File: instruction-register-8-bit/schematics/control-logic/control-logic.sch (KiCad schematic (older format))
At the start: 6 parts

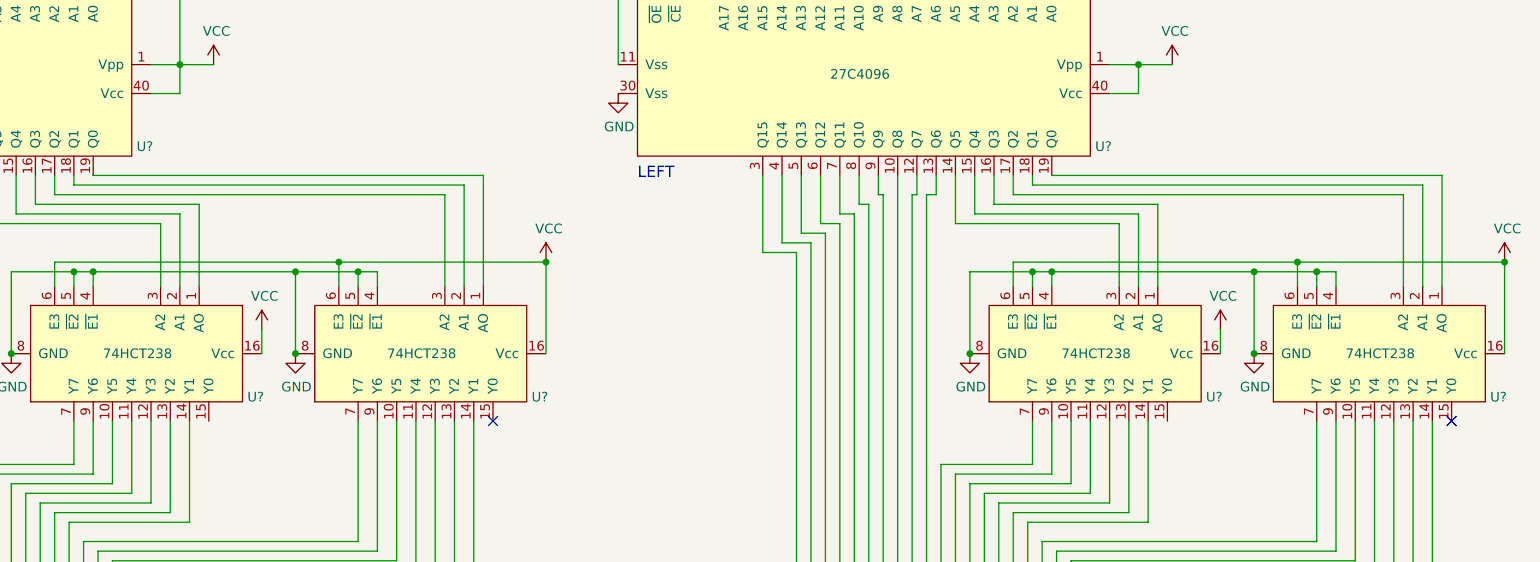
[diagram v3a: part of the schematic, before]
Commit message: removed A16 address line
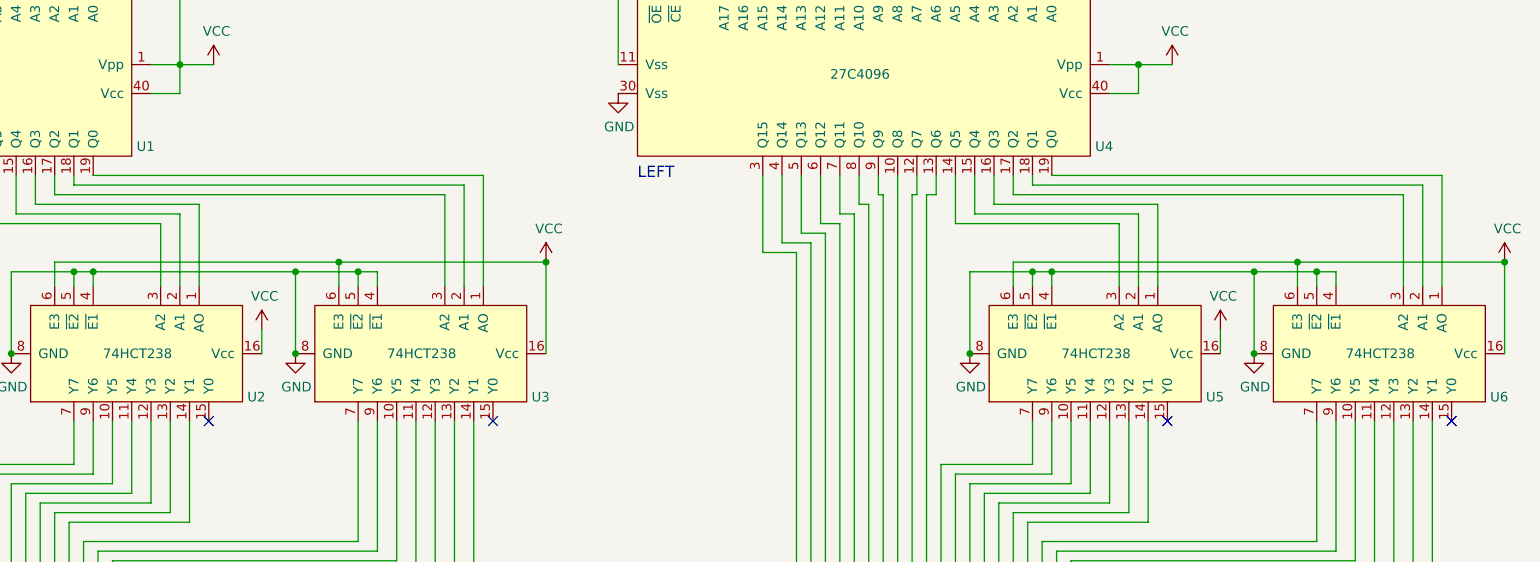
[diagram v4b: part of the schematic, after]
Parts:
- gave numbers to parts that had none: 6
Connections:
- no-connect marks 2 -> 4
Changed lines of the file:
@@
 $EndDescr
 $Comp
-L common-symbols:74HCT238 U?
+L common-symbols:74HCT238 U3
 U 1 1 60DA7B46
 P 5450 4825
-F 0 "U?" V 5675 5375 50  0000 L CNN
+F 0 "U3" V 5675 5375 50  0000 L CNN
 F 1 "74HCT238" V 5450 4625 50  0000 L CNN
 F 2 "" H 5300 4650 50  0001 C CNN
@@
 $EndComp
 $Comp
-L common-symbols:74HCT238 U?
+L common-symbols:74HCT238 U2
 U 1 1 60D8B240
 P 3975 4825
-F 0 "U?" V 4200 5375 50  0000 L CNN
+F 0 "U2" V 4200 5375 50  0000 L CNN
 F 1 "74HCT238" V 3975 4625 50  0000 L CNN
 F 2 "" H 3825 4650 50  0001 C CNN
@@
 CL_48
 $Comp
-L power:GND #PWR?
+L power:GND #PWR01
 U 1 1 60E3EE03
 P 1475 3475
-F 0 "#PWR?" H 1475 3225 50  0001 C CNN
+F 0 "#PWR01" H 1475 3225 50  0001 C CNN
 F 1 "GND" H 1480 3302 50  0000 C CNN
 F 2 "" H 1475 3475 50  0001 C CNN
@@
 $EndComp
 $Comp
-L power:GND #PWR?
+L power:GND #PWR05
 U 1 1 60E3F44C
 P 4775 4825
-F 0 "#PWR?" H 4775 4575 50  0001 C CNN
+F 0 "#PWR05" H 4775 4575 50  0001 C CNN
 F 1 "GND" H 4780 4652 50  0000 C CNN
 F 2 "" H 4775 4825 50  0001 C CNN
@@
 $EndComp
 $Comp
-L power:VCC #PWR?
+L power:VCC #PWR04
 U 1 1 60E3F8E0
 P 4600 4700
-F 0 "#PWR?" H 4600 4550 50  0001 C CNN
+F 0 "#PWR04" H 4600 4550 50  0001 C CNN
 F 1 "VCC" H 4615 4873 50  0000 C CNN
 F 2 "" H 4600 4700 50  0001 C CNN
@@
 	4600 4825 4600 4700
 $Comp
-L power:VCC #PWR?
+L power:VCC #PWR06
 U 1 1 60E4BA0B
 P 6075 4350
-F 0 "#PWR?" H 6075 4200 50  0001 C CNN
+F 0 "#PWR06" H 6075 4200 50  0001 C CNN
 F 1 "VCC" H 6090 4523 50  0000 C CNN
 F 2 "" H 6075 4350 50  0001 C CNN
@@
 	4175 3325 4350 3325
 $Comp
-L power:VCC #PWR?
+L power:VCC #PWR03
 U 1 1 6128F265
 P 4350 3325
-F 0 "#PWR?" H 4350 3175 50  0001 C CNN
+F 0 "#PWR03" H 4350 3175 50  0001 C CNN
 F 1 "VCC" H 4365 3498 50  0000 C CNN
 F 2 "" H 4350 3325 50  0001 C CNN
@@
 	1475 2800 1475 3325
 $Comp
-L common-symbols:27C4096 U?
+L common-symbols:27C4096 U1
 U 1 1 60DAC648
 P 3925 2975
-F 0 "U?" V 4700 3000 50  0000 L CNN
+F 0 "U1" V 4700 3000 50  0000 L CNN
 F 1 "27C4096" V 4325 1625 50  0000 L CNN
 F 2 "" H 4000 2900 50  0001 C CNN
@@
 Connection ~ 5100 4400
 $Comp
-L power:GND #PWR?
+L power:GND #PWR02
 U 1 1 6126E82E
 P 3300 4825
-F 0 "#PWR?" H 3300 4575 50  0001 C CNN
+F 0 "#PWR02" H 3300 4575 50  0001 C CNN
 F 1 "GND" H 3305 4652 50  0000 C CNN
 F 2 "" H 3300 4825 50  0001 C CNN
@@
 	3600 5700 4225 5700
 $Comp
-L common-symbols:74HCT238 U?
+L common-symbols:74HCT238 U6
 U 1 1 61437C3F
 P 10425 4825
-F 0 "U?" V 10650 5375 50  0000 L CNN
+F 0 "U6" V 10650 5375 50  0000 L CNN
 F 1 "74HCT238" V 10425 4625 50  0000 L CNN
 F 2 "" H 10275 4650 50  0001 C CNN
@@
 $EndComp
 $Comp
-L common-symbols:74HCT238 U?
+L common-symbols:74HCT238 U5
 U 1 1 61437C45
 P 8950 4825
-F 0 "U?" V 9175 5375 50  0000 L CNN
+F 0 "U5" V 9175 5375 50  0000 L CNN
 F 1 "74HCT238" V 8950 4625 50  0000 L CNN
 F 2 "" H 8800 4650 50  0001 C CNN
@@
 NoConn ~ 10775 5175
 $Comp
-L power:GND #PWR?
+L power:GND #PWR07
 U 1 1 61437C88
 P 6450 3475
-F 0 "#PWR?" H 6450 3225 50  0001 C CNN
+F 0 "#PWR07" H 6450 3225 50  0001 C CNN
 F 1 "GND" H 6455 3302 50  0000 C CNN
 F 2 "" H 6450 3475 50  0001 C CNN
@@
 $EndComp
 $Comp
-L power:GND #PWR?
+L power:GND #PWR011
 U 1 1 61437C8E
 P 9750 4825
-F 0 "#PWR?" H 9750 4575 50  0001 C CNN
+F 0 "#PWR011" H 9750 4575 50  0001 C CNN
 F 1 "GND" H 9755 4652 50  0000 C CNN
 F 2 "" H 9750 4825 50  0001 C CNN
@@
 $EndComp
 $Comp
-L power:VCC #PWR?
+L power:VCC #PWR010
 U 1 1 61437C94
 P 9575 4700
-F 0 "#PWR?" H 9575 4550 50  0001 C CNN
+F 0 "#PWR010" H 9575 4550 50  0001 C CNN
 F 1 "VCC" H 9590 4873 50  0000 C CNN
 F 2 "" H 9575 4700 50  0001 C CNN
@@
 	9575 4825 9575 4700
 $Comp
-L power:VCC #PWR?
+L power:VCC #PWR012
 U 1 1 61437C9B
 P 11050 4350
-F 0 "#PWR?" H 11050 4200 50  0001 C CNN
+F 0 "#PWR012" H 11050 4200 50  0001 C CNN
 F 1 "VCC" H 11065 4523 50  0000 C CNN
 F 2 "" H 11050 4350 50  0001 C CNN
@@
 	9150 3325 9325 3325
 $Comp
-L power:VCC #PWR?
+L power:VCC #PWR09
 U 1 1 61437CB7
 P 9325 3325
-F 0 "#PWR?" H 9325 3175 50  0001 C CNN
+F 0 "#PWR09" H 9325 3175 50  0001 C CNN
 F 1 "VCC" H 9340 3498 50  0000 C CNN
 F 2 "" H 9325 3325 50  0001 C CNN
@@
 	6450 2800 6450 3325
 $Comp
-L common-symbols:27C4096 U?
+L common-symbols:27C4096 U4
 U 1 1 61437CC3
 P 8900 2975
-F 0 "U?" V 9675 3000 50  0000 L CNN
+F 0 "U4" V 9675 3000 50  0000 L CNN
 F 1 "27C4096" V 9300 1625 50  0000 L CNN
 F 2 "" H 8975 2900 50  0001 C CNN
@@
 Connection ~ 10075 4400
 $Comp
-L power:GND #PWR?
+L power:GND #PWR08
 U 1 1 61437CE8
 P 8275 4825
-F 0 "#PWR?" H 8275 4575 50  0001 C CNN
+F 0 "#PWR08" H 8275 4575 50  0001 C CNN
 F 1 "GND" H 8280 4652 50  0000 C CNN
 F 2 "" H 8275 4825 50  0001 C CNN
@@
 Wire Wire Line
 	2225 1850 2225 2875
+NoConn ~ 4325 5175
+NoConn ~ 9300 5175
 $EndSCHEMATC
